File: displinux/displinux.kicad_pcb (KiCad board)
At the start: 2 copper layers, 165 parts, among them J11 Conn_02x03_Odd_Even, J12 Conn_02x17_Odd_Even, J13 Conn_01x02, J15 HR911105A, J2 AudioJack4, J3 AudioJack4, J5 Conn_01x04, J6 Conn_01x06, J7 Conn_01x40_MountingPin, J8 Conn_01x24_MountingPin, J9 Conn_01x03, U1 SY8089AAAC, U2 SY8089AAAC, U3 SY8089AAAC, U4 SY7201ABC, U5 F133, U6 XC6206PxxxMR, U7 W25N01KV, U8 DP83848C, X1 ASE-50MHz, Y1 24M, Y2 Crystal

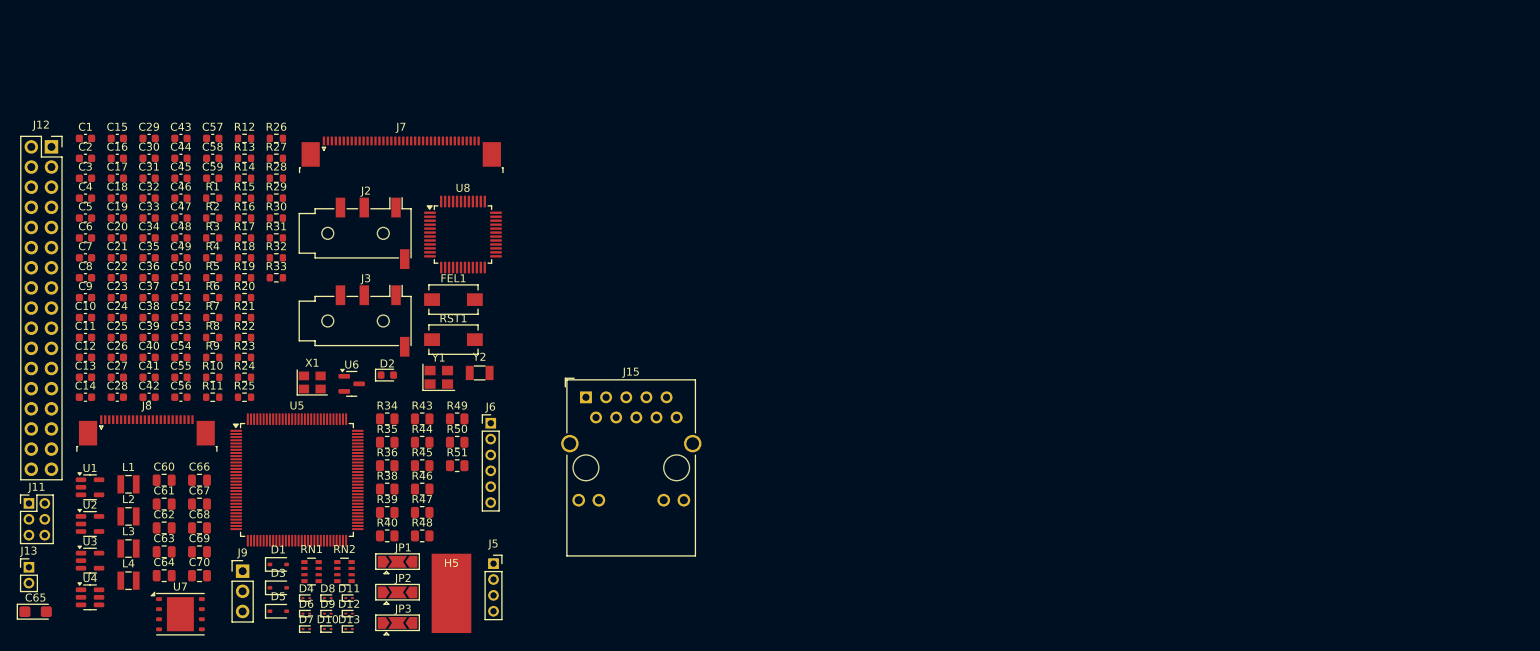
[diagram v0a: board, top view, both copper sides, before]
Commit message: add schematic
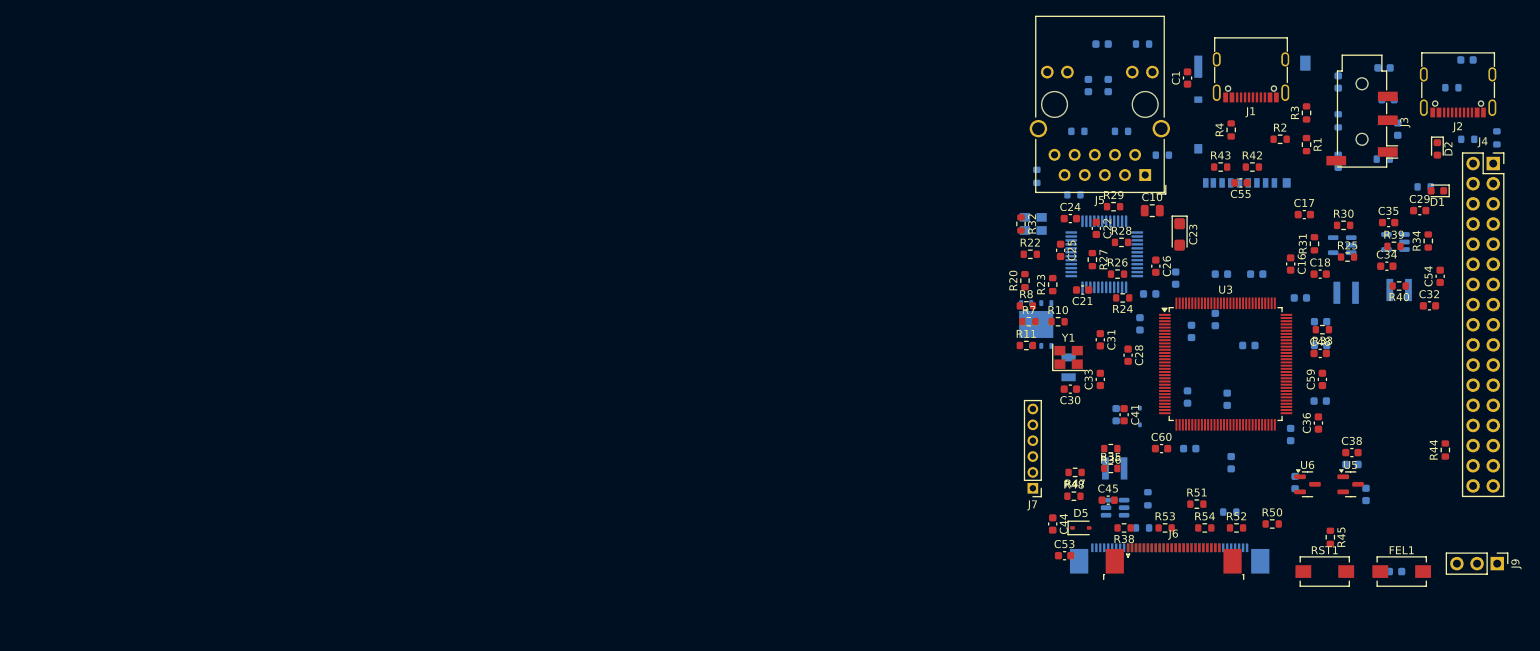
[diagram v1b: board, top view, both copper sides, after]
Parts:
- removed C13: 10u, Capacitor_SMD:C_0603_1608Metric
- removed C14: 0.1u, Capacitor_SMD:C_0603_1608Metric
- removed C64, C66, C67, C68, C69, C70: 0.1uF, Capacitor_SMD:C_0805_2012Metric
- removed C65: 10uF, Capacitor_Tantalum_SMD:CP_EIA-3216-10_Kemet-I
- removed D10, D11, D12, D13, D4, D6, D7, D8, D9: ESD9B3.3ST5G, Diode_SMD:D_SOD-923
- removed H5: MountingHole_Pad, Connector_Wire:SolderWirePad_1x01_SMD_5x10mm
- removed J11: Conn_02x03_Odd_Even, Connector_PinHeader_2.00mm:PinHeader_2x03_P2.00mm_Vertical
- removed J12: Conn_02x17_Odd_Even, Connector_PinSocket_2.54mm:PinSocket_2x17_P2.54mm_Vertical
- removed J13: Conn_01x02, Connector_PinHeader_2.00mm:PinHeader_1x02_P2.00mm_Vertical
- removed J15: HR911105A, Connector_RJ:RJ45_Wuerth_7499111446_Horizontal
- removed JP1, JP2, JP3: Jumper_3_Open, Jumper:SolderJumper-3_P2.0mm_Open_TrianglePad1.0x1.5mm
- removed L4: 2.2u, Inductor_SMD:L_Wuerth_MAPI-2510
- removed RN1, RN2: R_Pack04, Resistor_SMD:R_Array_Convex_4x0603
- added J1: USB4105-GF-A, Connector_USB:USB_C_Receptacle_G-Switch_GT-USB-7010ASV, F.Cu at (242.5, 53.0)
- added J4: Conn_02x17_Odd_Even, Connector_PinSocket_2.54mm:PinSocket_2x17_P2.54mm_Vertical, F.Cu at (273.0, 65.1)
- added R41: 240, Resistor_SMD:R_0603_1608Metric, B.Cu at (239.8, 109.0)
- added R42: 2.2K, Resistor_SMD:R_0603_1608Metric, F.Cu at (242.7, 65.5)
- added R52: 10k, Resistor_SMD:R_0603_1608Metric, F.Cu at (240.7, 111.0)
- added R53: 10k, Resistor_SMD:R_0603_1608Metric, F.Cu at (231.7, 111.0)
- added R54: 10k, Resistor_SMD:R_0603_1608Metric, F.Cu at (236.7, 111.0)
- added XS1: uSD_SMD, Connector_Card:microSD_HC_Hirose_DM3AT-SF-PEJM5, B.Cu at (242.7, 59.8)
- C10: value 0.1u -> 0.1uF; footprint Capacitor_SMD:C_0603_1608Metric -> Capacitor_SMD:C_0805_2012Metric
- C11: value 10u -> 0.1uF; moved to B.Cu
- C12, C46, C5, C52, C58, C6, C7: value 10u -> 0.1u; moved to B.Cu
- C15, C2, C3, C37, C39, C4, C40, C43, C49, C50, C51, C56, C57, D3, R9, U2, X1, Y2: moved to B.Cu
- C16, C17, C32, C38, C45, C53: value 0.1u -> 10u
- C19, C27: value 0.1u -> 0.47u; moved to B.Cu
- C20, C8, C9: value 0.1u -> 0.1uF; moved to B.Cu
- C21, C22, C24, C25, C26: value 0.1u -> 0.1uF
- C23: value 18p -> 10uF; footprint Capacitor_SMD:C_0603_1608Metric -> Capacitor_Tantalum_SMD:CP_EIA-3216-10_Kemet-I
- C28: value 33p -> 18p
- C29: value 18p -> 0.1u
- C33: value 0.1u -> 18p
- C42: value 0.1u -> 10u; moved to B.Cu
- C47: value 1u -> 0.1u; moved to B.Cu
- C48: value 1u -> 0.1u
- C54, C55: value 0.47u -> 0.1u
- C60: value 0.1uF -> 0.1u; footprint Capacitor_SMD:C_0805_2012Metric -> Capacitor_SMD:C_0603_1608Metric
- C61, C62, C63: value 0.1uF -> 0.1u; footprint Capacitor_SMD:C_0805_2012Metric -> Capacitor_SMD:C_0603_1608Metric; moved to B.Cu
- D1: value D -> LED; footprint Diode_SMD:D_SOD-323 -> LED_SMD:LED_0603_1608Metric
- J2: value AudioJack4 -> USB4105-GF-A; footprint Connector_Audio:Jack_3.5mm_PJ320D_Horizontal -> Connector_USB:USB_C_Receptacle_G-Switch_GT-USB-7010ASV
- J5: value Conn_01x04 -> HR911105A; footprint Connector_PinSocket_2.00mm:PinSocket_1x04_P2.00mm_Vertical -> Connector_RJ:RJ45_Wuerth_7499111446_Horizontal
- J6: value Conn_01x06 -> Conn_01x24_MountingPin; footprint Connector_PinHeader_2.00mm:PinHeader_1x06_P2.00mm_Vertical -> Connector_FFC-FPC:TE_2-1734839-4_1x24-1MP_P0.5mm_Horizontal
- J7: value Conn_01x40_MountingPin -> Conn_01x06; footprint Connector_FFC-FPC:TE_4-1734839-0_1x40-1MP_P0.5mm_Horizontal -> Connector_PinHeader_2.00mm:PinHeader_1x06_P2.00mm_Vertical
- J8: value Conn_01x24_MountingPin -> Conn_01x40_MountingPin; footprint Connector_FFC-FPC:TE_2-1734839-4_1x24-1MP_P0.5mm_Horizontal -> Connector_FFC-FPC:TE_4-1734839-0_1x40-1MP_P0.5mm_Horizontal; moved to B.Cu
- L1: value 10u -> 2.2u; footprint Inductor_SMD:L_Wuerth_MAPI-2510 -> Inductor_SMD_Wurth:L_Wurth_WE-LQSH-3012; moved to B.Cu
- L2: footprint Inductor_SMD:L_Wuerth_MAPI-2510 -> Inductor_SMD_Wurth:L_Wurth_WE-LQSH-3012; moved to B.Cu
- L3: value 2.2u -> 10u; footprint Inductor_SMD:L_Wuerth_MAPI-2510 -> Inductor_SMD_Wurth:L_Wurth_WE-LQSH-3012; moved to B.Cu
- R1: value 1k -> 5.1k
- R10, R11: value 2R2 -> 10k
- R12: value 10k -> 2R2; moved to B.Cu
- R13, R16: value 10k -> 49R9; moved to B.Cu
- R14: value 5.1k -> 49R9; moved to B.Cu
- R15: value 100k -> 49R9; moved to B.Cu
- R17: value 10k -> 5.1k; moved to B.Cu
- R18: value 2.2k -> 7.87k; moved to B.Cu
- R19: value 10M -> 220; moved to B.Cu
- R2: value 10k -> 5.1k
- R20: value 240 -> 2.2K
- R21: value 5.1k -> 220; moved to B.Cu
- R22: value 0 -> 2.2K
- R23, R26, R27: value 5.1k -> 2.2K
- R24, R28: value 10k -> 2.2K
- R25: value 10k -> 1k
- R29: value 10k -> 4.87K
- R3: value 15k -> 5.1k
- R30: value 5.1k -> 15k
- R31: value 10k -> 68k
- R32: value 10k -> 10K
- R33: value 5.1k -> 0
- R34: value 10K -> 10k; footprint Resistor_SMD:R_0805_2012Metric -> Resistor_SMD:R_0603_1608Metric
- R35, R36, R47, R48: value 2.2K -> 10k; footprint Resistor_SMD:R_0805_2012Metric -> Resistor_SMD:R_0603_1608Metric
- R38: value 2.2K -> 1k; footprint Resistor_SMD:R_0805_2012Metric -> Resistor_SMD:R_0603_1608Metric
- R39: value 2.2K -> 200k; footprint Resistor_SMD:R_0805_2012Metric -> Resistor_SMD:R_0603_1608Metric
- R4: value 100k -> 5.1k
- R40: value 2.2K -> 100k; footprint Resistor_SMD:R_0805_2012Metric -> Resistor_SMD:R_0603_1608Metric
- R43, R44: value 49R9 -> 2.2K; footprint Resistor_SMD:R_0805_2012Metric -> Resistor_SMD:R_0603_1608Metric
- R45: value 49R9 -> 100k; footprint Resistor_SMD:R_0805_2012Metric -> Resistor_SMD:R_0603_1608Metric
- R46: value 49R9 -> 2R2; footprint Resistor_SMD:R_0805_2012Metric -> Resistor_SMD:R_0603_1608Metric; moved to B.Cu
- R49: value 4.87K -> 10k; footprint Resistor_SMD:R_0805_2012Metric -> Resistor_SMD:R_0603_1608Metric; moved to B.Cu
- R5: value 200k -> 5.1k; moved to B.Cu
- R50, R51: value 220 -> 10k; footprint Resistor_SMD:R_0805_2012Metric -> Resistor_SMD:R_0603_1608Metric
- R6: value 68k -> 5.1k; moved to B.Cu
- R7: value 200k -> 10k
- R8: value 100k -> 10k
- U1: value SY8089AAAC -> DP83848C; footprint Package_TO_SOT_SMD:SOT-23-5 -> Package_QFP:LQFP-48_7x7mm_P0.5mm; moved to B.Cu
- U3: value SY8089AAAC -> F133; footprint Package_TO_SOT_SMD:SOT-23-5 -> Package_QFP:LQFP-128_14x14mm_P0.4mm
- U4: value SY7201ABC -> SY8089AAAC; footprint Package_TO_SOT_SMD:SOT-23-6 -> Package_TO_SOT_SMD:SOT-23-5; moved to B.Cu
- U5: value F133 -> XC6206P_2_8_MR; footprint Package_QFP:LQFP-128_14x14mm_P0.4mm -> Package_TO_SOT_SMD:SOT-23
- U6: value XC6206PxxxMR -> XC6206P_1_2_MR
- U7: value W25N01KV -> SY7201ABC; footprint Package_SON:WSON-8-1EP_6x5mm_P1.27mm_EP3.4x4.3mm -> Package_TO_SOT_SMD:SOT-23-6; moved to B.Cu
- U8: value DP83848C -> W25N01KV; footprint Package_QFP:LQFP-48_7x7mm_P0.5mm -> Package_SON:WSON-8-1EP_6x5mm_P1.27mm_EP3.4x4.3mm; moved to B.Cu
- moved C2 174.6 mm to (269.7, 52.0)
- moved U4 170.6 mm to (260.7, 75.0), turned to 180 degrees
- moved C6 166.0 mm to (261.0, 60.7), turned to -90 degrees
- moved C5 164.8 mm to (259.3, 53.0), turned to 180 degrees
- moved C4 164.7 mm to (259.8, 57.0), turned to 180 degrees
- moved R5 162.9 mm to (273.5, 61.8), turned to 90 degrees
- moved L2 162.7 mm to (261.2, 81.0), turned to 180 degrees
- moved C32 162.0 mm to (265.0, 83.0)
- moved U2 161.7 mm to (254.0, 75.3), turned to 180 degrees
- moved C29 160.5 mm to (263.8, 71.0)
- moved C7 159.5 mm to (253.5, 54.8), turned to 90 degrees
- moved C54 159.1 mm to (266.4, 79.3), turned to 90 degrees
- moved R6 158.5 mm to (267.8, 55.5), turned to 180 degrees
- moved J9 158.2 mm to (273.5, 115.5), turned to -90 degrees
- moved C3 158.0 mm to (253.5, 64.8), turned to 90 degrees
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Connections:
- C1 pad 1: /LCD_A -> +5V
- C10 pad 1: /VDD-CORE -> +3V3
- C11 pad 1: +5V -> +3V3
- C12 pad 1: +5V -> GND
- C12 pad 2: GND -> +3V3
- C15 pad 1: GND -> +3V3
- C15 pad 2: Net-(C15-Pad2) -> GND
- C16 pad 1: /VDD-CORE -> +5V
- C17 pad 1: +1V8 -> +3V3
- C18 pad 1: /RST -> +3V3
- C19 pad 1: /VDD-CORE -> GND
- C19 pad 2: GND -> Net-(U3-VRA1)
- C20 pad 1: +1V8 -> Net-(U1-PFBIN1)
- C21 pad 1: /VDD-CORE -> Net-(U1-PFBIN1)
- C22 pad 1: +1V8 -> Net-(U1-PFBIN1)
- C23 pad 1: GND -> Net-(U1-PFBIN1)
- C23 pad 2: /DXIN -> GND
- C24 pad 1: /MIC3P -> +3V3
- C24 pad 2: /HS_MIC -> GND
- C25 pad 1: /MIC3N -> +3V3
- C26 pad 1: /VDD-CORE -> +3V3
- C27 pad 1: +1V8 -> GND
- C27 pad 2: GND -> Net-(U3-VRA2)
- C28 pad 1: /HS_MIC -> /DXOUT
- C29 pad 1: /DXOUT -> Net-(U4-EN)
- C3 pad 1: Net-(U2-EN) -> GND
- C3 pad 2: GND -> Net-(C3-Pad2)
- C30 pad 1: Net-(U5-X32KOUT) -> GND
- C30 pad 2: GND -> /DXIN
- C31 pad 1: Net-(U5-XX32KIN) -> Net-(U3-X32KOUT)
- C32 pad 1: +1V8 -> +5V
- C33 pad 1: +3V3 -> Net-(U3-XX32KIN)
- C34 pad 1: +1V8 -> /VDD-CORE
- C35 pad 1: +1V8 -> /VDD-CORE
- C36 pad 1: +3V3 -> GND
- C36 pad 2: GND -> +3V3
- C38 pad 1: +3V3 -> GND
- C38 pad 2: GND -> +3V3
- C39 pad 1: +1V8 -> /CSI-DVDD-2_8V
- C4 pad 1: /LCD_A -> Net-(C4-Pad1)
- C4 pad 2: GND -> /HPOUTR
- C40 pad 1: +3V3 -> +1V8
- C41 pad 1: /HPOUTFB -> /LDOB-OUT
- C42 pad 1: /LDOB-OUT -> GND
- C42 pad 2: GND -> +3V3
- C43 pad 1: GND -> /CSI-DVDD-1_2V
- C43 pad 2: /VCC_PG -> GND
- C44 pad 1: Net-(D6-A2) -> +3V3
- C44 pad 2: /HPOUTR -> GND
- C45 pad 1: Net-(D7-A2) -> +5V
- C45 pad 2: /HPOUTL -> GND
- C46 pad 1: GND -> /VDD-CORE
- C46 pad 2: +3V3 -> GND
- C47 pad 1: Net-(U5-TVIN-VRN) -> /VDD-CORE
- C48 pad 1: Net-(U5-TVIN-VRP) -> /VDD-CORE
- C49 pad 1: Net-(D8-A2) -> /VDD-CORE
- C49 pad 2: /LINEL -> GND
- C5 pad 1: +3V3 -> /HPOUTFB
- C50 pad 1: Net-(D9-A2) -> +3V3
- C50 pad 2: /LINER -> GND
- C51 pad 1: /CSI-DVDD -> +3V3
- C52 pad 1: +5V -> +3V3
- C53 pad 1: GND -> /LCD_A
- C53 pad 2: /VCC_PD -> GND
- C54 pad 1: GND -> /LCD_A
- C54 pad 2: Net-(U5-VRA1) -> GND
- C55 pad 1: GND -> +3V3
- C55 pad 2: Net-(U5-VRA2) -> GND
- C56 pad 1: +3V3 -> /RST
- C57 pad 1: +3V3 -> +1V8
- C58 pad 1: +5V -> +1V8
- C59 pad 1: /CSI-AVDD -> +1V8
- C6 pad 1: +1V8 -> Net-(C6-Pad1)
- C6 pad 2: GND -> /HPOUTL
- C60 pad 1: +3V3 -> +1V8
- C61 pad 1: Net-(U8-PFBIN1) -> +1V8
- C62 pad 1: Net-(U8-PFBIN1) -> +1V8
- C63 pad 1: +3V3 -> +1V8
- C7 pad 1: /VDD-CORE -> GND
- C7 pad 2: GND -> Net-(C7-Pad2)
- C9 pad 1: +1V8 -> +3V3
- D1 pad 1: /LCD_A -> GND
- D3 pad 1: +5V -> Net-(D3-K)
- D5 pad 1: Net-(D5-K) -> /LCD_A
- D5 pad 2: +3V3 -> Net-(D5-A)
- FEL1 pad 2: /PC5 -> /SPI0_MISO
- J3 pad R1: Net-(D8-A2) -> Net-(C4-Pad1)
- J3 pad S: unconnected-(J3-PadS) -> /HS_MIC
- J3 pad T: Net-(D9-A2) -> Net-(C6-Pad1)
- J5 pad 1: /TP_X1 -> Net-(U1-TD+)
- J5 pad 2: /TP_Y1 -> Net-(U1-TD-)
- J5 pad 3: /TP_X2 -> Net-(U1-RD+)
- J5 pad 4: /TP_Y2 -> +3V3
- J6 pad 1: /GPADC0 -> unconnected-(J6-Pin_1-Pad1)
- J6 pad 2: /TP_X1 -> GND
- J6 pad 3: /TP_X2 -> /TWI2-SDA
- J6 pad 4: /TP_Y1 -> /CSI-DVDD-2_8V
- J6 pad 5: /TP_Y2 -> /TWI2-SCK
- J6 pad 6: GND -> /CSI-RST#
- J7 pad 1: /LCD_K -> /GPADC0
- J7 pad 2: /LCD_A -> /TP_X1
- J7 pad 3: GND -> /TP_Y1
- J7 pad 4: +3V3 -> /TP_X2
- J7 pad 5: /LCD0-D0 -> /TP_Y2
- J7 pad 6: /LCD0-D1 -> GND
- J8 pad 1: GND -> /LCD_K
- J8 pad 10: /CSI-AVDD -> /LCD0-D21
- J8 pad 11: GND -> /LCD0-D22
- J8 pad 12: Net-(J8-Pin_12) -> /LCD0-D23
- J8 pad 13: Net-(J8-Pin_13) -> /LCD0-D8
- J8 pad 14: GND -> /LCD0-D9
- J8 pad 15: /NCSI0-D7 -> /LCD0-D10
- J8 pad 16: /NCSI0-D6 -> /LCD0-D11
- J8 pad 17: /NCSI0-D5 -> /LCD0-D12
- J8 pad 18: /NCSI0-D4 -> /LCD0-D13
- J8 pad 19: /NCSI0-D3 -> /LCD0-D14
- J8 pad 2: /TWI2-SDA -> /LCD_A
- J8 pad 20: /NCSI0-D2 -> /LCD0-D15
- J8 pad 21: /NCSI0-D1 -> /LCD0-D0
- J8 pad 22: /NCSI0-D0 -> /LCD0-D1
- J8 pad 23: /CSI-IOVDD -> /LCD0-D2
- J8 pad 24: /CSI-IOVDD -> /LCD0-D3
- J8 pad 3: /TWI2-SCK -> GND
- J8 pad 4: /CSI-RST# -> +3V3
- J8 pad 5: /CSI-PWDN -> /LCD0-D16
- J8 pad 6: Net-(J8-Pin_6) -> /LCD0-D17
- J8 pad 7: Net-(J8-Pin_7) -> /LCD0-D18
- J8 pad 8: /CSI-DVDD -> /LCD0-D19
- J8 pad 9: /CSI-AVDD -> /LCD0-D20
- L1 pad 1: +5V -> +3V3
- L1 pad 2: Net-(D1-A) -> Net-(U2-LX)
- L2 pad 1: +3V3 -> /VDD-CORE
- L2 pad 2: Net-(U1-LX) -> Net-(U4-LX)
- L3 pad 1: +1V8 -> +5V
- L3 pad 2: Net-(U2-LX) -> Net-(D5-A)
- R1 pad 1: +5V -> Net-(J1-CC1)
- R1 pad 2: Net-(U1-EN) -> GND
- R10 pad 1: Net-(C14-Pad2) -> /SPI0_MOSI
- R10 pad 2: /HPOUTR -> GND
- R11 pad 1: Net-(C15-Pad2) -> /SPI0_MISO
- R11 pad 2: /HPOUTL -> GND
- R12 pad 1: +3V3 -> Net-(C7-Pad2)
- R12 pad 2: /PC4 -> /HPOUTL
- R13 pad 1: /PC4 -> +3V3
- R13 pad 2: GND -> Net-(U1-TD+)
- R14 pad 2: Net-(D2-A) -> Net-(U1-TD-)
- R15 pad 2: /RST -> Net-(U1-RD+)
- R16 pad 2: /PC5 -> Net-(U1-RD-)
- R17 pad 1: /PC5 -> +3V3
- R17 pad 2: GND -> Net-(D1-A)
- R18 pad 1: +1V8 -> +5V
- R18 pad 2: /HS_MIC -> Net-(D2-A)
- R19 pad 1: Net-(U5-X32KOUT) -> Net-(J5-Pad10)
- R19 pad 2: Net-(U5-XX32KIN) -> Net-(U1-AN0/LED_LINK)
- R2 pad 1: +3V3 -> +5V
- R2 pad 2: Net-(U2-EN) -> Net-(J1-CC1)
- R20 pad 1: Net-(U5-DZQ) -> Net-(U1-RX_DV/MII_MODE)
- R20 pad 2: GND -> +3V3
- R21 pad 1: Net-(J4-CC1) -> Net-(J5-Pad11)
- R21 pad 2: GND -> Net-(U1-AN_EN/LED_ACT/COL)
- R22 pad 1: GND -> +3V3
- R22 pad 2: Net-(U5-AGND) -> /PG14
- R23 pad 1: +5V -> +3V3
- R23 pad 2: Net-(J4-CC1) -> /PG15
- R24 pad 1: +3V3 -> Net-(U1-RX_DV/MII_MODE)
- R24 pad 2: /DISP -> /PG0
- R25 pad 1: /DISP -> +5V
- R25 pad 2: GND -> Net-(U2-EN)
- R26 pad 1: Net-(J4-CC2) -> +3V3
- R26 pad 2: GND -> Net-(R26-Pad2)
- R27 pad 1: +5V -> Net-(U1-~{RESET})
- R27 pad 2: Net-(J4-CC2) -> +3V3
- R28 pad 2: /CSI-PWDN -> Net-(R28-Pad2)
- R29 pad 1: /CSI-PWDN -> GND
- R29 pad 2: GND -> Net-(U1-RBIAS)
- R3 pad 1: Net-(U1-FB) -> Net-(J1-CC2)
- R30 pad 1: +5V -> Net-(U2-FB)
- R30 pad 2: Net-(J10-CC1) -> GND
- R31 pad 2: /CSI-RST# -> Net-(U2-FB)
- R32 pad 1: /CSI-RST# -> Net-(X1-EN)
- R32 pad 2: GND -> +3V3
- R33 pad 1: +5V -> GND
- R33 pad 2: Net-(J10-CC2) -> Net-(U3-AGND)
- R34 pad 1: Net-(X1-EN) -> +3V3
- R34 pad 2: +3V3 -> Net-(U4-EN)
- R35 pad 2: /PG14 -> /CSI-RST#
- R36 pad 1: +3V3 -> /CSI-RST#
- R36 pad 2: /PG15 -> GND
- R38 pad 1: Net-(U8-RX_DV/MII_MODE) -> /CSI-PWDN
- R38 pad 2: +3V3 -> GND
- R39 pad 1: Net-(U8-~{RESET}) -> Net-(U4-FB)
- R39 pad 2: +3V3 -> GND
- R4 pad 1: Net-(U2-FB) -> +5V
- R4 pad 2: GND -> Net-(J1-CC2)
- R40 pad 1: Net-(U8-RX_DV/MII_MODE) -> /VDD-CORE
- R40 pad 2: /PG0 -> Net-(U4-FB)
- R43 pad 2: Net-(U8-TD+) -> /SDC0-CD
- R44 pad 2: Net-(U8-TD-) -> /SPI0_CS0
- R45 pad 2: Net-(U8-RD+) -> /RST
- R46 pad 1: +3V3 -> /LCD_K
- R46 pad 2: Net-(U8-RD-) -> GND
- R47 pad 2: Net-(R47-Pad2) -> /DISP
- R48 pad 1: +3V3 -> /DISP
- R48 pad 2: Net-(R48-Pad2) -> GND
- R49 pad 1: GND -> +3V3
- R49 pad 2: Net-(U8-RBIAS) -> GND
- R5 pad 1: Net-(U3-FB) -> +5V
- R5 pad 2: GND -> Net-(J2-CC1)
- R50 pad 1: Net-(J15-Pad10) -> /LCD0-D17
- R50 pad 2: Net-(U8-AN0/LED_LINK) -> GND
- R51 pad 1: Net-(J15-Pad11) -> /LCD0-D8
- R51 pad 2: Net-(U8-AN_EN/LED_ACT/COL) -> GND
- R6 pad 1: +3V3 -> +5V
- R6 pad 2: Net-(U1-FB) -> Net-(J2-CC2)
- R7 pad 1: +1V8 -> +3V3
- R7 pad 2: Net-(U2-FB) -> /SPI0_MOSI
- R8 pad 1: /VDD-CORE -> +3V3
- R8 pad 2: Net-(U3-FB) -> /SPI0_MISO
- R9 pad 1: /LCD_K -> Net-(C3-Pad2)
- R9 pad 2: GND -> /HPOUTR
- U1 pad 1: Net-(U1-EN) -> unconnected-(U1-TX_CLK-Pad1)
- U1 pad 2: GND -> /PG12
- U1 pad 3: Net-(U1-LX) -> /PG4
- U1 pad 4: +5V -> /PG5
- U1 pad 5: Net-(U1-FB) -> unconnected-(U1-TXD_2-Pad5)
- U3 pad 1: Net-(U2-EN) -> /PG6
- U3 pad 2: GND -> /PG7
- U3 pad 3: Net-(U3-LX) -> /PG8
- U3 pad 4: +5V -> /PG9
- U3 pad 5: Net-(U3-FB) -> /PG10
- U4 pad 1: Net-(D1-A) -> Net-(U4-EN)
- U4 pad 3: /LCD_K -> Net-(U4-LX)
- U4 pad 4: /LCD0_PWM -> +5V
- U4 pad 5: /LCD_A -> Net-(U4-FB)
- U5 pad 1: /PG6 -> GND
- U5 pad 2: /PG7 -> /CSI-DVDD-2_8V
- U5 pad 3: /PG8 -> +3V3
- U6 pad 2: /CSI-DVDD -> /CSI-DVDD-1_2V
- U7 pad 1: /PC3 -> Net-(D5-A)
- U7 pad 2: /PC5 -> GND
- U7 pad 3: /PC6 -> /LCD_K
- U7 pad 4: GND -> /LCD0_PWM
- U7 pad 5: /PC4 -> /LCD_A
- U7 pad 6: /PC2 -> +5V
- U8 pad 1: unconnected-(U8-TX_CLK-Pad1) -> /SPI0_CS0
- U8 pad 2: /PG12 -> /SPI0_MISO
- U8 pad 3: /PG4 -> /SPI0_WP
- U8 pad 4: /PG5 -> GND
- U8 pad 5: unconnected-(U8-TXD_2-Pad5) -> /SPI0_MOSI
- U8 pad 6: unconnected-(U8-TXD_3/SNI_MODE-Pad6) -> /SPI0_CLK
- U8 pad 7: unconnected-(U8-PWR_DOWN/INT-Pad7) -> /SPI0_HOLD
- U8 pad 8: (no net) -> +3V3
- Y2 pad 1: Net-(U5-X32KOUT) -> Net-(U3-X32KOUT)
- Y2 pad 2: Net-(U5-XX32KIN) -> Net-(U3-XX32KIN)

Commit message: start tracing
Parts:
- added J10: Conn_01x03, Connector_PinHeader_2.54mm:PinHeader_1x03_P2.54mm_Vertical, F.Cu at (269.5, 79.7)
- C1, C17, C28, C30, C31, C33, C36, C38, C45, C48, C53, C54, C59, C60, FEL1, R1, R2, R20, R29, R3, R38, R4, R45, R48, R50, R51, R52, R53, R54, U5, U6: moved to B.Cu
- C10: footprint Capacitor_SMD:C_0805_2012Metric -> Capacitor_SMD:C_0603_1608Metric; moved to B.Cu
- C12, C2, J8, R17, R18, R5, R6: moved to F.Cu
- D3: footprint Diode_SMD:D_SOD-323 -> Diode_SMD:D_SOD-523
- D5: footprint Diode_SMD:D_SOD-323 -> Diode_SMD:D_SOD-523; moved to B.Cu
- J4: value Conn_02x17_Odd_Even -> Conn_02x10_Counter_Clockwise; footprint Connector_PinSocket_2.54mm:PinSocket_2x17_P2.54mm_Vertical -> Connector_PinHeader_2.54mm:PinHeader_2x10_P2.54mm_Vertical
- J5: footprint Connector_RJ:RJ45_Wuerth_7499111446_Horizontal -> Connector_RJ:RJ45_Hanrun_HR911105A_Horizontal
- J7: footprint Connector_PinHeader_2.00mm:PinHeader_1x06_P2.00mm_Vertical -> Connector_PinHeader_2.54mm:PinHeader_1x06_P2.54mm_Vertical
- J9: value Conn_01x03 -> Conn_01x02_Pin; footprint Connector_PinHeader_2.54mm:PinHeader_1x03_P2.54mm_Vertical -> Connector_PinHeader_2.54mm:PinHeader_1x02_P2.54mm_Vertical
- moved J4 59.4 mm to (215.5, 79.7)
- moved J7 56.9 mm to (269.5, 89.7), turned to 0 degrees
- moved J9 50.9 mm to (225.0, 100.0)
- moved R44 44.9 mm to (223.0, 92.2)
- moved FEL1 42.9 mm to (223.8, 96.0)
- moved R48 38.0 mm to (257.8, 112.7)
- moved R47 37.1 mm to (257.3, 106.3)
- moved C38 36.9 mm to (220.5, 114.0), turned to -90 degrees
- moved C1 36.2 mm to (270.5, 57.8), turned to -90 degrees
- moved C54 35.6 mm to (240.2, 103.4)
- moved C39 33.7 mm to (223.4, 108.4), turned to 180 degrees
- moved U5 33.1 mm to (223.0, 113.6), turned to -90 degrees
- moved C2 32.8 mm to (237.0, 54.0), turned to 90 degrees
- moved C56 32.8 mm to (230.9, 103.0), turned to 180 degrees
- moved C35 29.3 mm to (264.1, 101.5)
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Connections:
- J2 pad A1: (no net) -> GND
- J2 pad A12: (no net) -> GND
- J2 pad B1: (no net) -> GND
- J2 pad B12: (no net) -> GND
- J4 pad 10: /MIC3P -> /SPI0_WP
- J4 pad 11: unconnected-(J4-Pin_11-Pad11) -> /SPI0_MISO
- J4 pad 12: unconnected-(J4-Pin_12-Pad12) -> /SPI0_MOSI
- J4 pad 13: unconnected-(J4-Pin_13-Pad13) -> /SPI0_CS0
- J4 pad 14: unconnected-(J4-Pin_14-Pad14) -> /SPI0_CLK
- J4 pad 15: /PG6 -> /TWI2-SDA
- J4 pad 16: /PG7 -> /TWI2-SCK
- J4 pad 17: /PG8 -> /CLKO
- J4 pad 18: /PG9 -> GND
- J4 pad 19: /PG10 -> GND
- J4 pad 20: /PG11 -> GND
- J4 pad 3: +5V -> /PG6
- J4 pad 4: +3V3 -> /PG7
- J4 pad 5: /TWI2-SCK -> /PG8
- J4 pad 6: /TWI2-SDA -> /PG9
- J4 pad 7: /HPOUTFB -> /PG10
- J4 pad 8: /MIC3N -> /PG11
- J4 pad 9: unconnected-(J4-Pin_9-Pad9) -> /SPI0_HOLD
- J9 pad 1: GND -> /NCSI0-PCLK
- R24 pad 1: Net-(U1-RX_DV/MII_MODE) -> +3V3
- R49 pad 1: +3V3 -> /LCD0-D16
- U3 pad 125: /PG13 -> unconnected-(U3-PG13-Pad125)
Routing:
- net +3V3: track 0.00 -> 319.3 mm, vias 0 -> 30
- net +5V: track 0.00 -> 186.7 mm, vias 0 -> 5
- net /TP_X1: track 0.00 -> 68.0 mm, vias 0 -> 2
- net /TP_Y1: track 0.00 -> 61.9 mm, vias 0 -> 3
- net /TP_X2: track 0.00 -> 60.7 mm, vias 0 -> 3
- net /TP_Y2: track 0.00 -> 59.1 mm, vias 0 -> 3
- net +1V8: track 0.00 -> 57.6 mm, vias 0 -> 11
- net /VDD-CORE: track 0.00 -> 55.9 mm, vias 0 -> 6
- net /GPADC0: track 0.00 -> 41.4 mm, vias 0 -> 1
- net GND: track 0.00 -> 37.6 mm, vias 0 -> 7
- net /USB0_P: track 0.00 -> 34.7 mm, vias 0 -> 2
- net /USB0_N: track 0.00 -> 34.6 mm, vias 0 -> 2
- net /PG5: track 0.00 -> 34.1 mm, vias 0 -> 3
- net /PG12: track 0.00 -> 33.1 mm, vias 0 -> 3
- net /SDC0-CD: track 0.00 -> 32.7 mm, vias 0 -> 2
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
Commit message: tracing finished Need to check
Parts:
- added ?: , , F.Cu at (246.2, 89.9)
- C29, R34, R47: moved to B.Cu
- C45: moved to F.Cu
- D5: footprint Diode_SMD:D_SOD-523 -> Diode_SMD:D_0805_2012Metric
- moved R47 7.20 mm to (257.7, 113.5)
- moved C45 6.83 mm to (243.0, 104.1), turned to 0 degrees
- moved R34 1.59 mm to (265.3, 91.5)
- moved R44 1.53 mm to (223.1, 93.7), turned to -90 degrees
- moved C29 0.98 mm to (265.2, 89.7)
- moved L2 0.92 mm to (263.2, 100.4)
- moved R11 0.85 mm to (221.1, 85.3)
- moved U4 0.84 mm to (262.8, 94.9)
- moved R48 0.82 mm to (257.6, 111.9)
- moved C44 0.79 mm to (243.5, 108.2), turned to 90 degrees
- moved C34 0.64 mm to (262.8, 97.6)
- moved R39 0.57 mm to (263.3, 92.4)
- moved C35 0.57 mm to (264.7, 101.5)
- moved C26 0.45 mm to (234.2, 81.1)
- moved D5 0.28 mm to (245.9, 103.4)
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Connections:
- J2 pad A1: GND -> (no net)
- J2 pad A12: GND -> (no net)
- J2 pad B1: GND -> (no net)
- J2 pad B12: GND -> (no net)
- U8 pad 9: (no net) -> GND
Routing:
- net GND: track 37.6 -> 143.0 mm, vias 7 -> 120
- net /LCD0-D8: track 0.00 -> 56.8 mm, vias 0 -> 2
- net /LCD0-D9: track 0.00 -> 53.8 mm, vias 0 -> 3
- net /TWI2-SDA: track 0.00 -> 48.3 mm, vias 0 -> 4
- net /TWI2-SCK: track 0.00 -> 39.9 mm, vias 0 -> 4
- net /LCD0-D0: track 0.00 -> 37.2 mm, vias 0 -> 4
- net /LCD0-D1: track 0.00 -> 36.5 mm, vias 0 -> 4
- net /LCD0-DE: track 0.00 -> 34.4 mm
- net /LCD0-D16: track 0.00 -> 34.0 mm, vias 0 -> 5
- net /LCD0-D17: track 0.00 -> 33.0 mm, vias 0 -> 5
- net /NCSI0-MCLK: track 0.00 -> 32.1 mm, vias 0 -> 2
- net /LCD0-D23: track 0.00 -> 32.1 mm, vias 0 -> 6
- net /SPI0_CS0: track 17.7 -> 49.1 mm, vias 1 -> 2
- net /LCD0-D15: track 0.00 -> 30.4 mm, vias 0 -> 4
- net /NCSI0-VSYNC: track 0.00 -> 29.7 mm, vias 0 -> 2
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- added copper zone on B.Cu, net GND
- added copper zone on F.Cu, net GND
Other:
- board outline added: 57.9 x 65.4 mm
- board text added: "+3.3"
- board text added: "+5"
- board text added: "3n"
- board text added: "3p"
- board text added: "HOST"
- board text added: "OTG"
- board text added: "Rx"
- board text added: "Tx"
- board text added: "UNIDISP"
- board text added: "clk"
- board text added: "clk0"
- board text added: "cs0"
- board text added: "g10"
- board text added: "g11"
- board text added: "g6"
- board text added: "g7"
- board text added: "g8"
- board text added: "g9"
- board text added: "gnd"
- board text added: "hold"
- board text added: "iso"
- board text added: "osi"
- board text added: "sck"
- board text added: "sda"
- board text added: "wp"

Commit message: add some earth
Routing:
- net GND: track 143.0 -> 148.6 mm, vias 120 -> 122
- net /PG0: track 27.8 -> 27.3 mm
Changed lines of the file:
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@@
 	)
 	(via
+		(at 242.82 77.91)
+		(size 0.6)
+		(drill 0.3)
+		(layers "F.Cu" "B.Cu")
+		(free yes)
+		(net 1)
+	)
+	(via
 		(at 253.19 74.18)
 		(size 0.6)
@@
 	)
 	(via
+		(at 241 75)
+		(size 0.6)
+		(drill 0.3)
+		(layers "F.Cu" "B.Cu")
+		(free yes)
+		(net 1)
+	)
+	(via
 		(at 231.53 95.5)
 		(size 0.6)
@@
 	)
 	(segment
+		(start 240.69 78.04)
+		(end 240.35 77.7)
+		(width 0.3)
+		(layer "B.Cu")
+		(net 1)
+	)
+	(segment
 		(start 230.77 88.72)
 		(end 230.77 88.545)
@@
 	)
 	(segment
+		(start 240.34 75.66)
+		(end 241 75)
+		(width 0.3)
+		(layer "B.Cu")
+		(net 1)
+	)
+	(segment
 		(start 218 100)
 		(end 219.5 98.5)
@@
 	)
 	(segment
+		(start 240.35 77.52)
+		(end 240.34 77.51)
+		(width 0.3)
+		(layer "B.Cu")
+		(net 1)
+	)
+	(segment
 		(start 227.33 87.45)
 		(end 227.36 87.42)
@@
 	)
 	(segment
+		(start 240.35 77.7)
+		(end 240.35 77.52)
+		(width 0.3)
+		(layer "B.Cu")
+		(net 1)
+	)
+	(segment
 		(start 230.530001 87.200001)
 		(end 230.725 87.395)
@@
 	)
 	(segment
+		(start 242.82 77.91)
+		(end 242.69 78.04)
+		(width 0.3)
+		(layer "B.Cu")
+		(net 1)
+	)
+	(segment
 		(start 231.35 78.2)
 		(end 231.19 78.2)
@@
 	)
 	(segment
+		(start 242.69 78.04)
+		(end 240.69 78.04)
+		(width 0.3)
+		(layer "B.Cu")
+		(net 1)
+	)
+	(segment
+		(start 240.34 77.51)
+		(end 240.34 75.66)
+		(width 0.3)
+		(layer "B.Cu")
+		(net 1)
+	)
+	(segment
 		(start 231.91 78.8)
 		(end 231.59 78.8)
@@
 	)
 	(segment
-		(start 238.22 78.21)
-		(end 238.2 78.23)
+		(start 242.5 78.5)
+		(end 238.36 78.5)
 		(width 0.2)
 		(layer "F.Cu")
@@
 	)
 	(segment
-		(start 243.1625 82.2375)
-		(end 243.1625 78.5225)
+		(start 238.36 78.5)
+		(end 238.2 78.34)
 		(width 0.2)
 		(layer "F.Cu")
@@
 	)
 	(segment
-		(start 242.85 78.21)
-		(end 238.22 78.21)
-		(width 0.2)
-		(layer "F.Cu")
-		(net 120)
-	)
-	(segment
 		(start 238.2 78.34)
 		(end 238.09 78.34)
@@
 	)
 	(segment
-		(start 238.2 78.23)
-		(end 238.2 78.34)
-		(width 0.2)
-		(layer "F.Cu")
-		(net 120)
-	)
-	(segment
-		(start 243.1625 78.5225)
-		(end 242.85 78.21)
+		(start 243.1625 82.2375)
+		(end 243.1625 79.1625)
 		(width 0.2)
 		(layer "F.Cu")
@@
 		(net 120)
 	)
+	(segment
+		(start 243.1625 79.1625)
+		(end 242.5 78.5)
+		(width 0.2)
+		(layer "F.Cu")
+		(net 120)
+	)
 	(via
 		(at 238.2 78.34)
@@
 	)
 	(segment
-		(start 243.5625 82.2375)
-		(end 243.5625 77.6425)
-		(width 0.2)
-		(layer "F.Cu")
-		(net 137)
-	)
-	(segment
 		(start 230.98 79.314422)
 		(end 230.98 77.99)
@@
 	)
 	(segment
-		(start 243.5625 77.6425)
-		(end 242.48 76.56)
+		(start 243.5625 82.2375)
+		(end 243.5625 77.6025)
 		(width 0.2)
 		(layer "F.Cu")
@@
 	)
 	(segment
+		(start 241.96 76)
+		(end 237.98 76)
+		(width 0.2)
+		(layer "F.Cu")
+		(net 137)
+	)
+	(segment
 		(start 225.52 77.73)
 		(end 225.6 77.65)
@@
 	)
 	(segment
-		(start 242.48 76.56)
-		(end 237.42 76.56)
+		(start 237.42 76.56)
+		(end 237.25 76.62)
 		(width 0.2)
 		(layer "F.Cu")
@@
 	)
 	(segment
-		(start 237.42 76.56)
-		(end 237.25 76.62)
+		(start 237.3 76.56)
+		(end 237.36 76.56)
 		(width 0.2)
 		(layer "F.Cu")
@@
 	)
 	(segment
-		(start 237.3 76.56)
-		(end 237.36 76.56)
+		(start 230.14 77.15)
+		(end 225.91 77.15)
 		(width 0.2)
 		(layer "F.Cu")
@@
 	)
 	(segment
-		(start 230.14 77.15)
-		(end 225.91 77.15)
+		(start 243.5625 77.6025)
+		(end 241.96 76)
 		(width 0.2)
 		(layer "F.Cu")
@@
 	)
 	(segment
+		(start 237.98 76)
+		(end 237.42 76.56)
+		(width 0.2)
+		(layer "F.Cu")
+		(net 137)
+	)
+	(segment
 		(start 225.91 77.15)
 		(end 225.52 77.54)
@@
 	)
 	(segment
-		(start 237.87 77.24)
-		(end 237.51 77.6)
-		(width 0.2)
-		(layer "F.Cu")
-		(net 138)
-	)
-	(segment
 		(start 229.72 77.71)
 		(end 226.54 77.71)
@@
 	)
 	(segment
+		(start 237.87 77.24)
+		(end 237.51 77.6)
+		(width 0.2)
+		(layer "F.Cu")
+		(net 138)
+	)
+	(segment
 		(start 237.51 77.61)
 		(end 237.5 77.61)
@@
 	)
 	(segment
-		(start 240.75 77.24)
+		(start 241.5 77.24)
 		(end 237.87 77.24)
 		(width 0.2)
@@
 	)
 	(segment
+		(start 237.51 77.6)
+		(end 237.51 77.61)
+		(width 0.2)
+		(layer "F.Cu")
+		(net 138)
+	)
+	(segment
 		(start 237.5 77.61)
 		(end 237.52 77.59)
@@
 	)
 	(segment
-		(start 237.51 77.6)
-		(end 237.51 77.61)
-		(width 0.2)
-		(layer "F.Cu")
-		(net 138)
-	)
-	(segment
 		(start 230.33 78.32)
 		(end 229.72 77.71)
@@
 	)
 	(via
-		(at 240.75 77.24)
+		(at 241.5 77.24)
 		(size 0.6)
 		(drill 0.3)
@@
 	)
 	(segment
-		(start 243.63 76.44)
-		(end 243.23 76.44)
-		(width 0.2)
-		(layer "B.Cu")
-		(net 138)
-	)
-	(segment
 		(start 242.43 77.24)
-		(end 240.75 77.24)
+		(end 243.23 76.44)
 		(width 0.2)
 		(layer "B.Cu")
@@
 	)
 	(segment
+		(start 243.23 76.44)
+		(end 243.63 76.44)
+		(width 0.2)
+		(layer "B.Cu")
+		(net 138)
+	)
+	(segment
 		(start 230.88 80.28)
 		(end 236.354975 80.28)
@@
 	)
 	(segment
-		(start 243.23 76.44)
-		(end 242.57 77.1)
-		(width 0.2)
-		(layer "B.Cu")
-		(net 138)
-	)
-	(segment
-		(start 242.57 77.1)
+		(start 241.5 77.24)
 		(end 242.43 77.24)
 		(width 0.2)
